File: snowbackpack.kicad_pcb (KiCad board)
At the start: 2 copper layers, 39.6 x 18 mm, 86 parts, among them J10 Conn_01x01_Pin, J11 Conn_01x01_Pin, J13 Conn_01x01_Pin, J2 Conn_01x01_Pin, J3 Conn_01x01_Pin, J4 Conn_01x01_Pin, J5 Conn_01x01_Pin, J6 Conn_01x01_Pin, J7 Conn_01x01_Pin, J8 Conn_01x01_Pin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

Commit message: Updated silkscreen with snowflakes
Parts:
- added G***: LOGO, Custom:flake1, F.Cu at (107.0, 88.6)
- added G***: LOGO, Custom:flake2, F.Cu at (80.8, 83.8)
- added G***: LOGO, Custom:flake2, F.Cu at (110.2, 94.0)
- added G***: LOGO, Custom:flake1, B.Cu at (101.8, 92.6)
- added G***: LOGO, Custom:flake2, B.Cu at (90.0, 90.0)
- added G***: LOGO, Custom:flake1, B.Cu at (84.4, 92.0)
- added G***: LOGO, Custom:flake1, B.Cu at (77.8, 93.0)
- added G***: LOGO, Custom:flake2, B.Cu at (111.0, 94.2)
- added G***: LOGO, Custom:flake2, B.Cu at (107.8, 96.2)
- added G***: LOGO, Custom:flake2, B.Cu at (101.2, 86.0)
- added G***: LOGO, Custom:flake1, B.Cu at (80.2, 86.0)
- added G***: LOGO, Custom:flake2, F.Cu at (86.6, 84.0)
- added G***: LOGO, Custom:flake2, B.Cu at (86.4, 85.2)
- added G***: LOGO, Custom:flake2, B.Cu at (110.0, 85.0)
- added G***: LOGO, Custom:flake1, B.Cu at (93.8, 85.2)
- added G***: LOGO, Custom:flake1, B.Cu at (77.0, 85.0)
- added G***: LOGO, Custom:flake2, B.Cu at (104.2, 96.4)
- added G***: LOGO, Custom:flake2, B.Cu at (94.0, 91.8)
- added G***: LOGO, Custom:flake2, B.Cu at (83.2, 84.0)
- added G***: LOGO, Custom:flake2, B.Cu at (80.8, 89.8)
- added G***: LOGO, Custom:flake1, B.Cu at (100.4, 96.3)
- added G***: LOGO, Custom:flake1, B.Cu at (84.8, 87.8)
- added G***: LOGO, Custom:flake1, F.Cu at (93.8, 86.2)
- added G***: LOGO, Custom:flake2, B.Cu at (77.8, 96.4)
- added G***: LOGO, Custom:flake1, B.Cu at (106.2, 92.8)
- added G***: LOGO, Custom:flake1, B.Cu at (97.8, 84.4)
- added G***: LOGO, Custom:flake1, B.Cu at (97.4, 89.2)
- added G***: LOGO, Custom:flake2, B.Cu at (111.4, 88.8)
- added G***: LOGO, Custom:flake1, B.Cu at (107.8, 88.6)
- added G***: LOGO, Custom:flake2, B.Cu at (105.2, 84.6)
- added G***: LOGO, Custom:flake1, B.Cu at (91.6, 96.6)
- added G***: LOGO, Custom:flake2, B.Cu at (76.8, 89.2)
- added G***: LOGO, Custom:flake1, B.Cu at (103.8, 89.0)
- added G***: LOGO, Custom:flake2, F.Cu at (78.4, 87.6)
- added G***: LOGO, Custom:flake1, B.Cu at (95.8, 96.2)
- added G***: LOGO, Custom:flake1, B.Cu at (81.6, 97.6)
- added G***: LOGO, Custom:flake1, F.Cu at (75.6, 91.2)
- added G***: LOGO, Custom:flake2, F.Cu at (81.0, 98.2)
- added G***: LOGO, Custom:flake1, F.Cu at (77.6, 84.8)
- added G***: LOGO, Custom:flake2, F.Cu at (87.0, 89.4)
- added G***: LOGO, Custom:flake1, F.Cu at (106.0, 91.8)
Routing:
- net GND: vias 30 -> 33
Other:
- board text added: "Nora"
- board text added: "SnowBackpack"
- board text added: "⋆"

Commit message: Slightly reduce clutter on silkscreen
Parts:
- removed the G*** at (107.0, 88.6)
- removed the G*** at (101.8, 92.6)
- removed the G*** at (90.0, 90.0)
- removed the G*** at (107.8, 96.2)
- removed the G*** at (80.2, 86.0)
- removed the G*** at (86.6, 84.0)
- removed the G*** at (86.4, 85.2)
- removed the G*** at (110.0, 85.0)
- removed the G*** at (104.2, 96.4)
- removed the G*** at (80.8, 89.8)
- removed the G*** at (97.8, 84.4)
- removed the G*** at (76.8, 89.2)
- removed the G*** at (103.8, 89.0)
- removed the G*** at (95.8, 96.2)
- removed the G*** at (81.6, 97.6)
- removed the G*** at (81.0, 98.2)
- removed the G*** at (77.6, 84.8)
- moved G*** 8.40 mm to (104.4, 84.6)
- moved G*** 8.00 mm to (106.0, 96.4)
- moved G*** 6.17 mm to (110.8, 87.2)
- moved G*** 5.41 mm to (100.8, 91.4)
- moved G*** 5.39 mm to (89.4, 90.0)
- moved G*** 5.14 mm to (106.4, 90.0)
- moved G*** 4.16 mm to (82.4, 91.2)
- moved G*** 3.31 mm to (76.4, 90.0)
- moved G*** 2.86 mm to (98.6, 86.6)
- moved G*** 1.84 mm to (93.0, 97.8)
- moved G*** 1.56 mm to (95.2, 90.8)
- moved G*** 1.44 mm to (84.0, 85.2)
- moved G*** 1.06 mm to (101.4, 96.0)
- moved G*** 1.00 mm to (110.2, 94.8)
- moved G*** 0.63 mm to (77.6, 85.2)
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
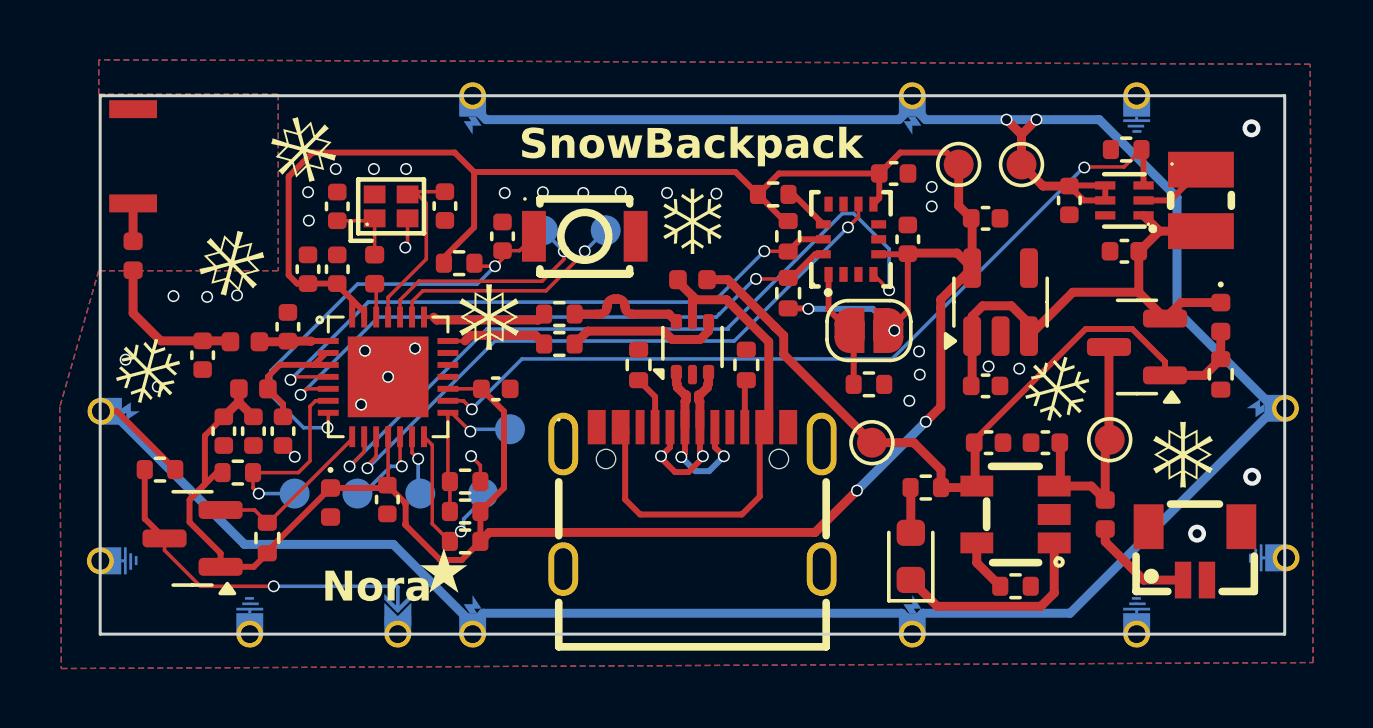
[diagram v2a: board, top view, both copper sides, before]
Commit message: Fixed interconnect spacing
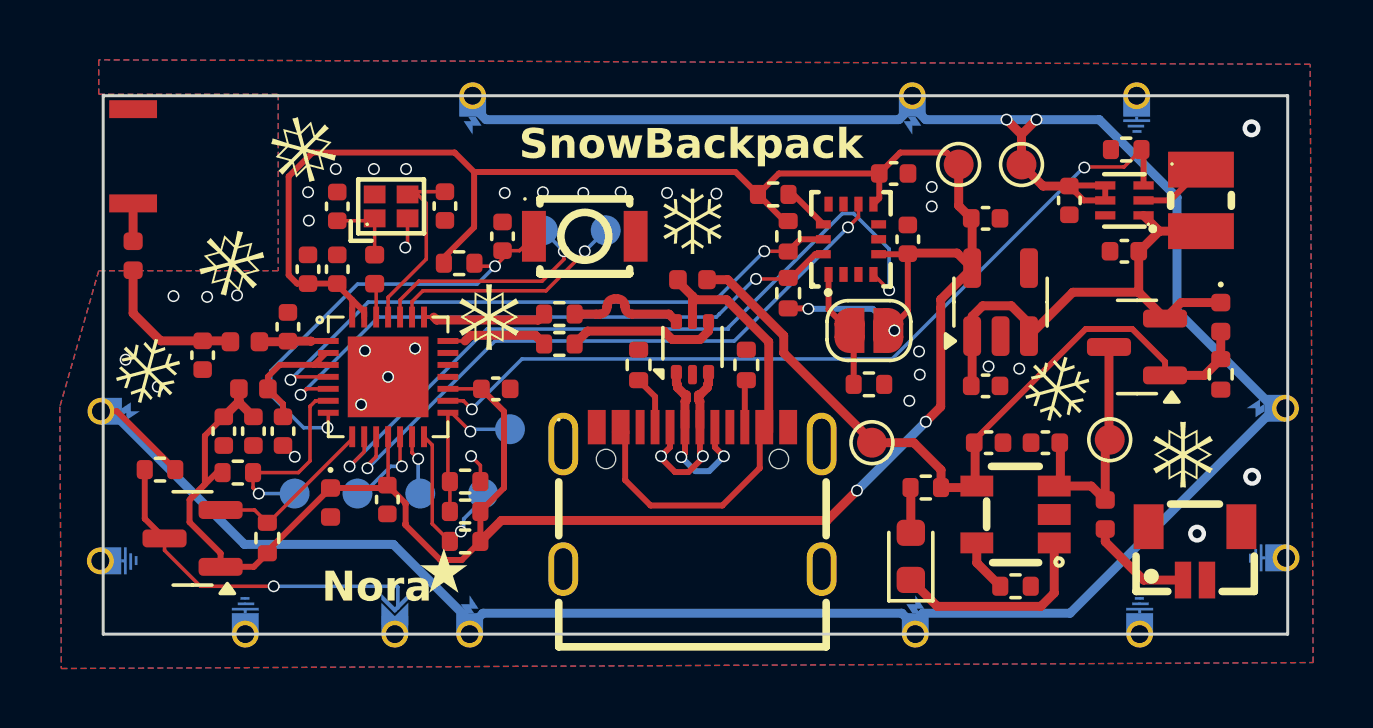
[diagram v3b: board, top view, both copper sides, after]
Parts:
- moved J4 0.15 mm to (78.8, 99.4)
- moved J13 0.10 mm to (108.7, 99.4)
- moved J5 0.10 mm to (86.3, 99.4)
- moved J9 0.10 mm to (101.2, 99.4)
- moved JP1 0.10 mm to (83.8, 99.4)
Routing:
- net VCCUSBC: track 17.5 -> 16.3 mm
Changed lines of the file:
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@@
 			(fill yes)
 			(layer "F.SilkS")
-			(net 27)
 		)
 		(embedded_fonts no)
@@
 			(fill yes)
 			(layer "B.SilkS")
-			(net 1353649920)
 		)
 		(embedded_fonts no)
@@
 			(fill yes)
 			(layer "B.SilkS")
-			(net 1903260017)
 		)
 		(embedded_fonts no)
@@
 			(fill yes)
 			(layer "B.SilkS")
-			(net 1353649920)
 		)
 		(embedded_fonts no)
@@
 	(footprint "Custom:matrix-pad-gn"
 		(layer "B.Cu")
-		(at 108.6 99.4 90)
+		(at 108.7 99.4 90)
 		(property "Reference" "J13"
 			(at 0.025 5.775 270)
@@
 	(footprint "Custom:matrix-pad-vcc"
 		(layer "B.Cu")
-		(at 101.1 99.4 90)
+		(at 101.2 99.4 90)
 		(property "Reference" "J9"
 			(at 0.025 5.775 270)
@@
 			(fill yes)
 			(layer "B.SilkS")
-			(net 31)
 		)
 		(embedded_fonts no)
@@
 			(fill yes)
 			(layer "B.SilkS")
-			(net 31)
 		)
 		(embedded_fonts no)
@@
 	(footprint "Custom:matrix-pad-gn"
 		(layer "B.Cu")
-		(at 78.95 99.4 90)
+		(at 78.8 99.4 90)
 		(property "Reference" "J4"
 			(at 0.025 5.775 270)
@@
 			(fill yes)
 			(layer "B.SilkS")
-			(net 119)
 		)
 		(embedded_fonts no)
@@
 			(fill yes)
 			(layer "B.SilkS")
-			(net 1903260017)
 		)
 		(embedded_fonts no)
@@
 			(fill yes)
 			(layer "B.SilkS")
-			(net 27)
 		)
 		(embedded_fonts no)
@@
 			(fill yes)
 			(layer "B.SilkS")
-			(net 86162439)
 		)
 		(embedded_fonts no)
@@
 			(fill yes)
 			(layer "B.SilkS")
-			(net 883149681)
 		)
 		(embedded_fonts no)
@@
 	(footprint "Custom:matrix-pad-vcc"
 		(layer "B.Cu")
-		(at 86.4 99.4 90)
+		(at 86.3 99.4 90)
 		(property "Reference" "J5"
 			(at 0.025 5.775 270)
@@
 			(fill yes)
 			(layer "B.SilkS")
-			(net 1718762912)
 		)
 		(embedded_fonts no)
@@
 	(footprint "Custom:matrix-pad-dout"
 		(layer "B.Cu")
-		(at 83.9 99.4 90)
+		(at 83.8 99.4 90)
 		(property "Reference" "JP1"
 			(at 0.025 5.775 270)
@@
 	)
 	(gr_rect
-		(start 74 82)
-		(end 113.6 100)
+		(start 74.1 82)
+		(end 113.7 100)
 		(stroke
 			(width 0.1)
@@
 	)
 	(segment
-		(start 99.3 95.2)
-		(end 97.9 96.6)
-		(width 0.3)
-		(layer "F.Cu")
-		(net 3)
-	)
-	(segment
 		(start 84.2 96.350337)
 		(end 85.370661 97.520998)
@@
 	)
 	(segment
-		(start 87.009997 96.6)
-		(end 86.709999 96.899998)
-		(width 0.3)
-		(layer "F.Cu")
-		(net 3)
-	)
-	(segment
 		(start 84.2 95.64245)
 		(end 84.211 95.65345)
@@
 	)
 	(segment
+		(start 87.409997 96.2)
+		(end 86.709999 96.899998)
+		(width 0.3)
+		(layer "F.Cu")
+		(net 3)
+	)
+	(segment
 		(start 82.425096 88.825096)
 		(end 82.425096 89.399999)
@@
 	)
 	(segment
+		(start 99.3 95.2)
+		(end 98.3 96.2)
+		(width 0.3)
+		(layer "F.Cu")
+		(net 3)
+	)
+	(segment
+		(start 98.3 96.2)
+		(end 87.409997 96.2)
+		(width 0.3)
+		(layer "F.Cu")
+		(net 3)
+	)
+	(segment
 		(start 77.895526 94.6)
 		(end 78.090001 94.6)
@@
 	)
 	(segment
-		(start 97.9 96.6)
-		(end 87.009997 96.6)
-		(width 0.3)
-		(layer "F.Cu")
-		(net 3)
-	)
-	(segment
 		(start 86.088999 97.520998)
 		(end 86.709999 96.899998)
@@
 	)
 	(segment
-		(start 96.557431 89.727861)
-		(end 96.850911 90.021342)
+		(start 94.285 88.15)
+		(end 94.97957 88.15)
 		(width 0.3)
 		(layer "F.Cu")
@@
 	)
 	(segment
-		(start 94.97957 88.15)
-		(end 96.557431 89.727861)
+		(start 99.8 93.55)
+		(end 99.8 93.6)
 		(width 0.3)
 		(layer "F.Cu")
@@
 	)
 	(segment
-		(start 96.850911 90.650911)
-		(end 99.8 93.6)
-		(width 0.3)
-		(layer "F.Cu")
-		(net 32)
-	)
-	(segment
 		(start 103.255119 95.1)
 		(end 103.305994 95.049125)
@@
 	)
 	(segment
-		(start 94.285 88.15)
-		(end 94.97957 88.15)
-		(width 0.3)
-		(layer "F.Cu")
-		(net 32)
-	)
-	(segment
 		(start 103.25 94.993131)
 		(end 103.25 93.630001)
@@
 	)
 	(segment
+		(start 96.850911 90.021342)
+		(end 96.850911 90.600911)
+		(width 0.3)
+		(layer "F.Cu")
+		(net 32)
+	)
+	(segment
 		(start 102.11 95.1)
 		(end 103.255119 95.1)
@@
 	)
 	(segment
+		(start 96.850911 90.600911)
+		(end 99.8 93.55)
+		(width 0.3)
+		(layer "F.Cu")
+		(net 32)
+	)
+	(segment
 		(start 103.22 93.525531)
 		(end 106.946531 89.799)
@@
 	)
 	(segment
-		(start 96.850911 90.021342)
-		(end 96.850911 90.650911)
+		(start 94.97957 88.15)
+		(end 96.850911 90.021342)
 		(width 0.3)
 		(layer "F.Cu")
@@
 	)
 	(segment
-		(start 96.049936 93.255016)
-		(end 96.049936 95.400064)
-		(width 0.2)
-		(layer "F.Cu")
-		(net 44)
-	)
-	(segment
-		(start 96.049936 95.400064)
-		(end 95.45 96)
-		(width 0.2)
-		(layer "F.Cu")
-		(net 44)
-	)
-	(segment
 		(start 93.8 89.475)
 		(end 93.8 88.7)
@@
 	)
 	(segment
+		(start 94.8 95.7)
+		(end 92.4 95.7)
+		(width 0.2)
+		(layer "F.Cu")
+		(net 44)
+	)
+	(segment
 		(start 94.942049 88.821)
 		(end 93.921 88.821)
@@
 	)
 	(segment
-		(start 91.550064 95.500064)
-		(end 91.550064 93.255016)
-		(width 0.2)
+		(start 93.921 88.821)
+		(end 93.8 88.7)
+		(width 0.3)
 		(layer "F.Cu")
 		(net 44)
 	)
 	(segment
-		(start 92.05 96)
-		(end 91.550064 95.500064)
+		(start 92.4 95.7)
+		(end 91.550064 94.850064)
 		(width 0.2)
 		(layer "F.Cu")
@@
 	)
 	(segment
-		(start 93.921 88.821)
-		(end 93.8 88.7)
-		(width 0.3)
+		(start 93.751 89.475)
+		(end 93.751 89.5)
+		(width 0.2)
 		(layer "F.Cu")
 		(net 44)
 	)
 	(segment
-		(start 93.751 89.475)
-		(end 93.751 89.5)
+		(start 91.550064 94.850064)
+		(end 91.550064 93.255016)
 		(width 0.2)
 		(layer "F.Cu")
@@
 	)
 	(segment
-		(start 95.45 96)
-		(end 92.05 96)
+		(start 96.049936 93.255016)
+		(end 96.049936 94.450064)
 		(width 0.2)
 		(layer "F.Cu")
@@
 		(width 0.2)
 		(layer "F.Cu")
+		(net 44)
+	)
+	(segment
+		(start 96.049936 94.450064)
+		(end 94.8 95.7)
+		(width 0.2)
+		(layer "F.Cu")

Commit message: Added v1 gerber files
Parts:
- moved F2 0.60 mm to (93.8, 87.5)
- moved R11 0.25 mm to (92.0, 91.2)
- moved R10 0.20 mm to (95.6, 91.2)
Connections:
- U2 pad 1: /USBCD+ -> /USBCD-
- U2 pad 3: /USBCD- -> /USBCD+
- U2 pad 4: /USBD- -> /USBD+
- U2 pad 6: /USBD+ -> /USBD-
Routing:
- net /USBCD+: track 6.00 -> 3.69 mm, vias 2 -> 0
- net VCCUSBC: track 16.3 -> 18.4 mm
- net /USBCD-: track 6.03 -> 4.39 mm, vias 2 -> 0
- net /USBD+: track 4.07 -> 5.19 mm
- net /USBD-: track 5.21 -> 5.71 mm
- net GND: vias 33 -> 47

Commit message: added BOM and cleaned up schematics
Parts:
- C10, C5, C8: value 0.1u -> 100n
- R10, R11: value 5.1K -> 5.1k
- R15, R2, R3, R5: value 10K -> 10k
- R4: value 5K -> 5k
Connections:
- net /USBCD+ renamed USBCD+
- net /USBCD- renamed USBCD-
- net /USBD+ renamed USBD+
- net /USBD- renamed USBD-
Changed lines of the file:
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@@
 	(net 50 "unconnected-(JP1-A-Pad1)_1")
 	(net 51 "unconnected-(AE1-FEED-Pad1)")
-	(net 52 "/USBD+")
-	(net 53 "/USBD-")
-	(net 54 "/USBCD-")
-	(net 55 "/USBCD+")
+	(net 52 "USBD+")
+	(net 53 "USBD-")
+	(net 54 "USBCD+")
+	(net 55 "USBCD-")
 	(footprint "Resistor_SMD:R_0402_1005Metric"
 		(layer "F.Cu")
@@
 			(layers "F.Cu" "F.Mask" "F.Paste")
 			(roundrect_rratio 0.25)
-			(net 52 "/USBD+")
+			(net 52 "USBD+")
 			(pintype "passive")
 		)
@@
 			)
 		)
-		(property "Value" "5.1K"
+		(property "Value" "5.1k"
 			(at 0 1.17 90)
 			(layer "F.Fab")
@@
 		(sheetfile "snowbackpack.kicad_sch")
 		(zone_connect 1)
-		(attr exclude_from_pos_files allow_soldermask_bridges)
+		(attr exclude_from_pos_files exclude_from_bom allow_soldermask_bridges)
 		(fp_poly
 			(pts
@@
 			)
 		)
-		(property "Value" "10K"
+		(property "Value" "10k"
 			(at 0 1.17 0)
 			(layer "F.Fab")
@@
 			)
 		)
-		(property "Value" "5K"
+		(property "Value" "5k"
 			(at 0 1.17 0)
 			(layer "F.Fab")
@@
 			)
 		)
-		(property "Value" "10K"
+		(property "Value" "10k"
 			(at 0 1.17 90)
 			(layer "F.Fab")
@@
 			(layers "F.Cu" "F.Mask" "F.Paste")
 			(roundrect_rratio 0.25)
-			(net 54 "/USBCD-")
+			(net 55 "USBCD-")
 			(pinfunction "I/O1")
 			(pintype "passive")
@@
 			(layers "F.Cu" "F.Mask" "F.Paste")
 			(roundrect_rratio 0.25)
-			(net 55 "/USBCD+")
+			(net 54 "USBCD+")
 			(pinfunction "I/O2")
 			(pintype "passive")
@@
 			(layers "F.Cu" "F.Mask" "F.Paste")
 			(roundrect_rratio 0.25)
-			(net 52 "/USBD+")
+			(net 52 "USBD+")
 			(pinfunction "I/O2")
 			(pintype "passive")
@@
 			(layers "F.Cu" "F.Mask" "F.Paste")
 			(roundrect_rratio 0.25)
-			(net 53 "/USBD-")
+			(net 53 "USBD-")
 			(pinfunction "I/O1")
 			(pintype "passive")
@@
 			)
 		)
-		(property "Value" "10K"
+		(property "Value" "10k"
 			(at 0 1.17 0)
 			(layer "F.Fab")
@@
 			)
 		)
-		(property "Value" "10K"
+		(property "Value" "10k"
 			(at 0 1.17 90)
 			(layer "F.Fab")
@@
 			)
 		)
-		(property "Value" "0.1u"
+		(property "Value" "100n"
 			(at 0 1.16 90)
 			(layer "F.Fab")
@@
 			)
 		)
-		(property "Value" "0.1u"
+		(property "Value" "100n"
 			(at 0 1.16 0)
 			(layer "F.Fab")
@@
 			)
 		)
-		(property "Value" "5.1K"
+		(property "Value" "5.1k"
 			(at 0 1.17 90)
 			(layer "F.Fab")
@@
 			(layers "F.Cu" "F.Mask" "F.Paste")
 			(roundrect_rratio 0.25)
-			(net 53 "/USBD-")
+			(net 53 "USBD-")
 			(pintype "passive")
 		)
@@
 			(size 0.3 1.150013)
 			(layers "F.Cu" "F.Mask" "F.Paste")
-			(net 55 "/USBCD+")
+			(net 54 "USBCD+")
 			(pinfunction "DP1")
 			(pintype "unspecified")
@@
 			(size 0.3 1.150013)
 			(layers "F.Cu" "F.Mask" "F.Paste")
-			(net 54 "/USBCD-")
+			(net 55 "USBCD-")
 			(pinfunction "DN1")
 			(pintype "unspecified")
@@
 			(size 0.3 1.150013)
 			(layers "F.Cu" "F.Mask" "F.Paste")
-			(net 55 "/USBCD+")
+			(net 54 "USBCD+")
 			(pinfunction "DP2")
 			(pintype "unspecified")
@@
 			(size 0.3 1.150013)
 			(layers "F.Cu" "F.Mask" "F.Paste")
-			(net 54 "/USBCD-")
+			(net 55 "USBCD-")
 			(pinfunction "DN2")
 			(pintype "unspecified")
@@
 			)
 		)
-		(property "Value" "0.1u"
+		(property "Value" "100n"
 			(at 0 1.16 90)
 			(layer "F.Fab")
@@
 	)
 	(segment
-		(start 94.049936 93.80715)
-		(end 93.951064 93.906022)
+		(start 93.550064 92.352882)
+		(end 93.652946 92.25)
 		(width 0.3)
 		(layer "F.Cu")
@@
 	)
 	(segment
-		(start 93.2625 91.25)
-		(end 93.051064 91.461436)
+		(start 93.652946 92.25)
+		(end 94.548936 92.25)
 		(width 0.3)
 		(layer "F.Cu")
@@
 	)
 	(segment
-		(start 93.051064 91.461436)
-		(end 93.051064 93.078888)
+		(start 94.548936 91.461436)
+		(end 94.548936 92.25)
 		(width 0.3)
 		(layer "F.Cu")
@@
 	)
 	(segment
-		(start 93.051064 93.7)
-		(end 93.051064 93.080016)
+		(start 94.3375 91.25)
+		(end 94.548936 91.461436)
 		(width 0.3)
 		(layer "F.Cu")
@@
 	)
 	(segment
-		(start 93.257086 93.906022)
-		(end 93.051064 93.7)
+		(start 93.550064 93.080016)
+		(end 93.550064 92.352882)
 		(width 0.3)
 		(layer "F.Cu")
@@
 	)
 	(segment
-		(start 94.049936 93.080016)
-		(end 94.049936 93.80715)
+		(start 94.548936 92.25)
+		(end 94.548936 93.078888)
 		(width 0.3)
 		(layer "F.Cu")
@@
 	)
 	(segment
-		(start 93.951064 93.906022)
-		(end 93.257086 93.906022)
+		(start 94.049936 93.80715)
+		(end 93.951064 93.906022)
 		(width 0.3)
 		(layer "F.Cu")
-		(net 54)
+		(net 55)
 	)
 	(segment
-		(start 93.550064 92.352882)
-		(end 93.652946 92.25)
+		(start 93.2625 91.25)
+		(end 93.051064 91.461436)
 		(width 0.3)
 		(layer "F.Cu")
@@
 	)
 	(segment
-		(start 93.652946 92.25)
-		(end 94.548936 92.25)
+		(start 93.051064 91.461436)
+		(end 93.051064 93.078888)
 		(width 0.3)
 		(layer "F.Cu")
@@
 	)
 	(segment
-		(start 94.548936 91.461436)
-		(end 94.548936 92.25)
+		(start 93.051064 93.7)
+		(end 93.051064 93.080016)
 		(width 0.3)
 		(layer "F.Cu")
@@
 	)
 	(segment
-		(start 94.3375 91.25)
-		(end 94.548936 91.461436)
+		(start 93.257086 93.906022)
+		(end 93.051064 93.7)
 		(width 0.3)
 		(layer "F.Cu")
@@
 	)
 	(segment
-		(start 93.550064 93.080016)
-		(end 93.550064 92.352882)
+		(start 94.049936 93.080016)
+		(end 94.049936 93.80715)
 		(width 0.3)
 		(layer "F.Cu")
@@
 	)
 	(segment
-		(start 94.548936 92.25)
-		(end 94.548936 93.078888)
+		(start 93.951064 93.906022)
+		(end 93.257086 93.906022)
 		(width 0.3)
 		(layer "F.Cu")

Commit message: Updated BOM
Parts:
- D2: value PTVS5V0Z1USK -> KLXES15AAA1
- D4: value D_Schottky -> RB161QS-40T18R
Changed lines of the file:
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@@
 			)
 		)
-		(property "Value" "D_Schottky"
+		(property "Value" "RB161QS-40T18R"
 			(at 0 1.17 90)
 			(layer "F.Fab")
@@
 			)
 		)
-		(property "Value" "PTVS5V0Z1USK"
+		(property "Value" "KLXES15AAA1"
 			(at 0 1.17 90)
 			(layer "F.Fab")
@@
 		(sheetname "/")
 		(sheetfile "snowbackpack.kicad_sch")
-		(attr exclude_from_pos_files)
+		(attr exclude_from_pos_files exclude_from_bom)
 		(fp_circle
 			(center 0 0)
@@
 		(sheetname "/")
 		(sheetfile "snowbackpack.kicad_sch")
-		(attr exclude_from_pos_files)
+		(attr exclude_from_pos_files exclude_from_bom)
 		(fp_circle
 			(center 0 0)
@@
 		(sheetname "/")
 		(sheetfile "snowbackpack.kicad_sch")
-		(attr exclude_from_pos_files)
+		(attr exclude_from_pos_files exclude_from_bom)
 		(fp_circle
 			(center 0 0)
@@
 		(sheetname "/")
 		(sheetfile "snowbackpack.kicad_sch")
-		(attr exclude_from_pos_files)
+		(attr exclude_from_pos_files exclude_from_bom)
 		(fp_circle
 			(center 0 0)
